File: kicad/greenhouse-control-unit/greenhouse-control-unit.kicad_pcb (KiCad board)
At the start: 2 copper layers, 85 parts, among them J1 Pluggable_Terminal_01x02, J10 Molex_KK-254_01x10, J10_LittleBuck1 Conn_01x01_Female, J11_LittleBuck1 Conn_01x01_Female, J12_BigBuck1 Conn_01x01_Female, J13_BigBuck1 Conn_01x01_Female, J14_LittleBuck1 Conn_01x01_Female, J15_LittleBuck1 Conn_01x01_Female, J2 Pluggable_Terminal_01x02, J3 Pluggable_Terminal_01x02, J4 Molex_KK-254_01x08, J5 Conn_01x10_Female, J6 Conn_01x10_Female, J6_BigBuck1 Conn_01x01_Female, J7 Conn_01x15_Female, J7_BigBuck1 Conn_01x01_Female, J8 Conn_01x15_Female, J9 Molex_KK-396_01x16, Q1 2N7000, Q10 IRLB8721PBF, Q11 IRLB8721PBF, Q12 D44H8, Q2 2N7000, Q3 2N2222A, Q4 IRLB8721PBF, Q5 IRLB8721PBF, Q6 IRLB8721PBF, Q7 IRLB8721PBF, Q8 IRLB8721PBF, Q9 IRLB8721PBF, U1 74HC595, U2 74HC595, U3 L298HN, U4 WS78L10

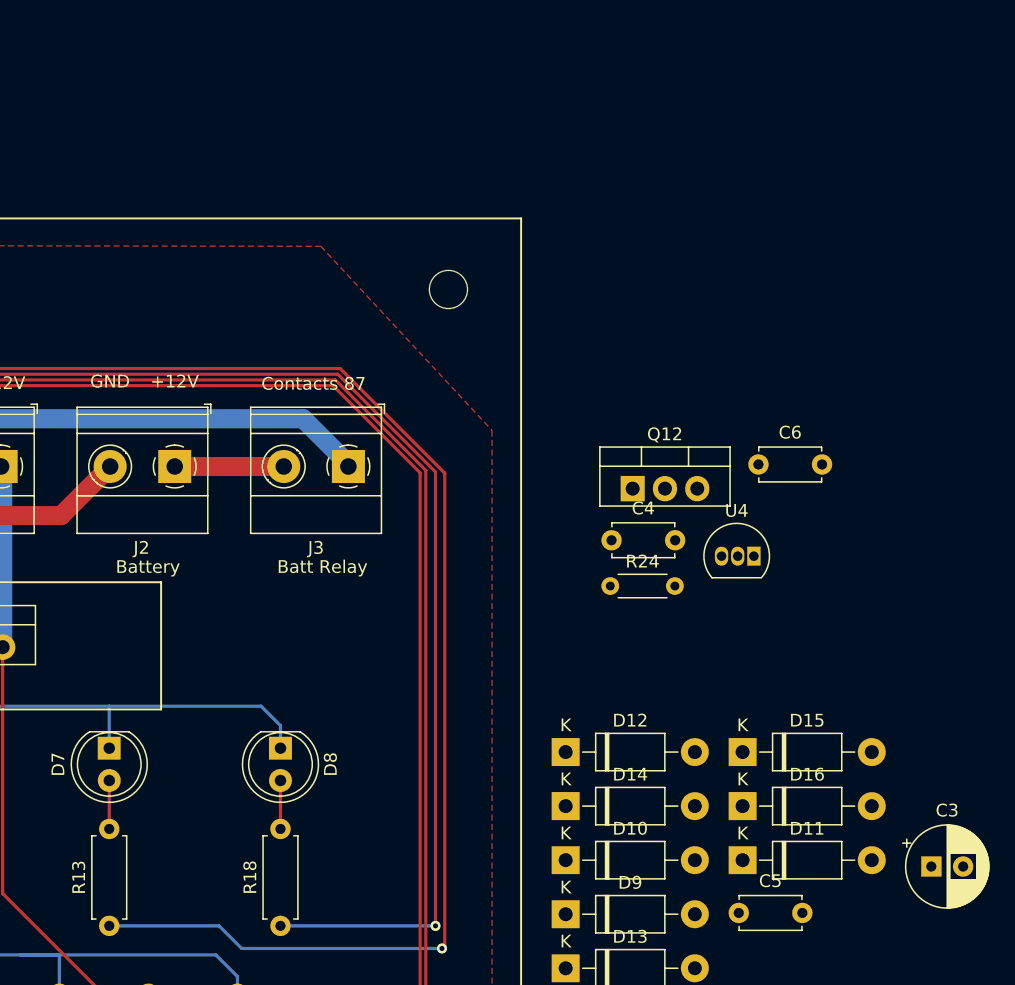
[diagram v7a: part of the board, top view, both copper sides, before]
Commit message: Change cap for motor driver regulator
Also moved battery coil to PSU #236
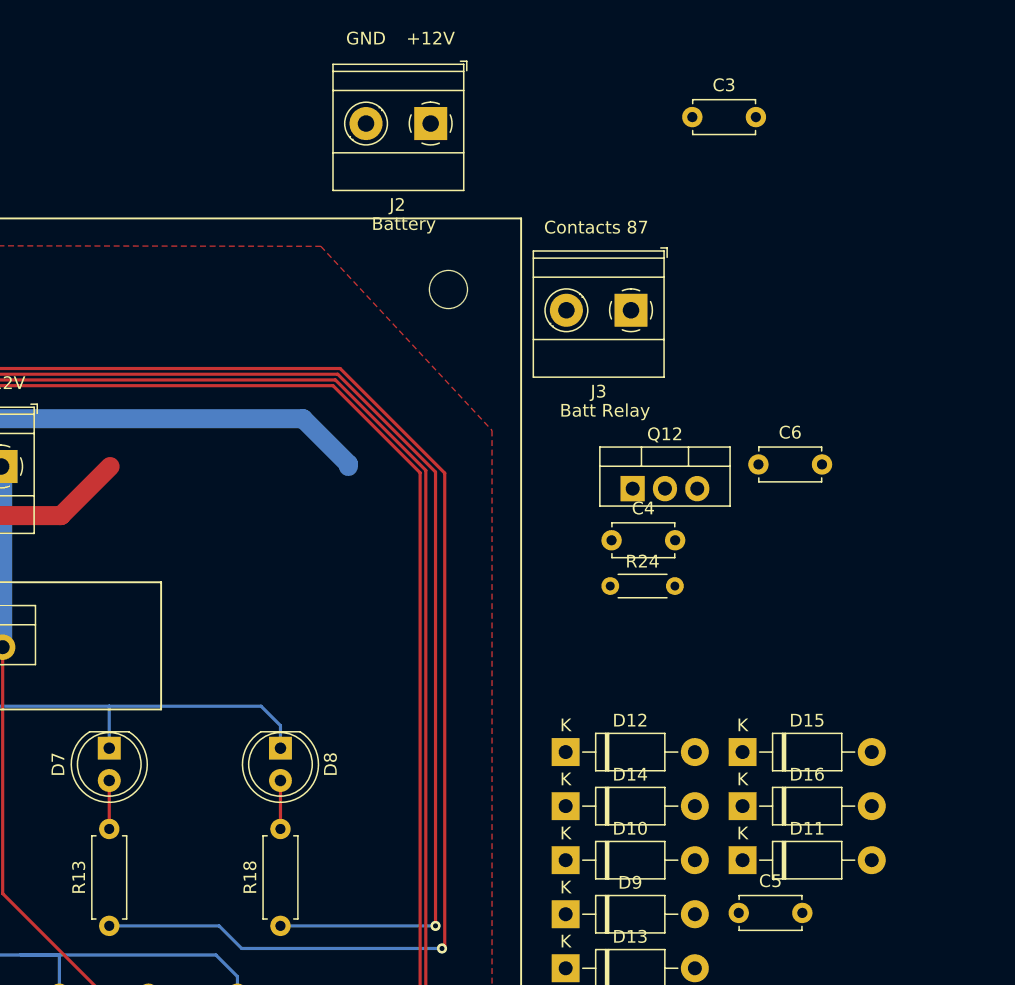
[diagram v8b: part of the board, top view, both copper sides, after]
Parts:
- removed U4: WS78L10, Nick:TO-92L_Inline_China
- C3: value 220uF -> 100nF; footprint Capacitor_THT:CP_Radial_D6.3mm_P2.50mm -> Capacitor_THT:C_Disc_D4.7mm_W2.5mm_P5.00mm
- moved C3 61.9 mm to (268.5, 17.3)
- moved J2 33.6 mm to (247.9, 17.8)
- moved J3 25.4 mm to (263.7, 32.5)
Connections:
- C3 pad 1: /L298N motor driver/Motor+10V -> GND
- C3 pad 2: GND -> +5V
- C5 pad 1: +5V -> /L298N motor driver/Motor+10V
- D1 pad 2: /PSU+12V -> /BattRelayNC_Coil
- J1 pad 1: /PSU+12V -> /BattRelayNC_Coil
- R1 pad 1: /PSU+12V -> /BattRelayNC_Coil
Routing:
- net /PSU+12V: track 48.4 -> 0.00 mm
- net /BattRelayNC_Coil: track 27.1 -> 75.4 mm
- net /Batt+12V: track 8.57 -> 0.00 mm
